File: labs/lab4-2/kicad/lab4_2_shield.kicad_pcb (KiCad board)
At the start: 2 copper layers, 68.6 x 53.3 mm, 35 parts, among them J1 Digital_0-7, J2 Digital_8-13, J3 Power, J4 Analog_In, Q1 2N3904, Q2 2N3904, SW1 SW_Push, SW2 SW_Push, SW3 SW_Push, SW4 SW_Push

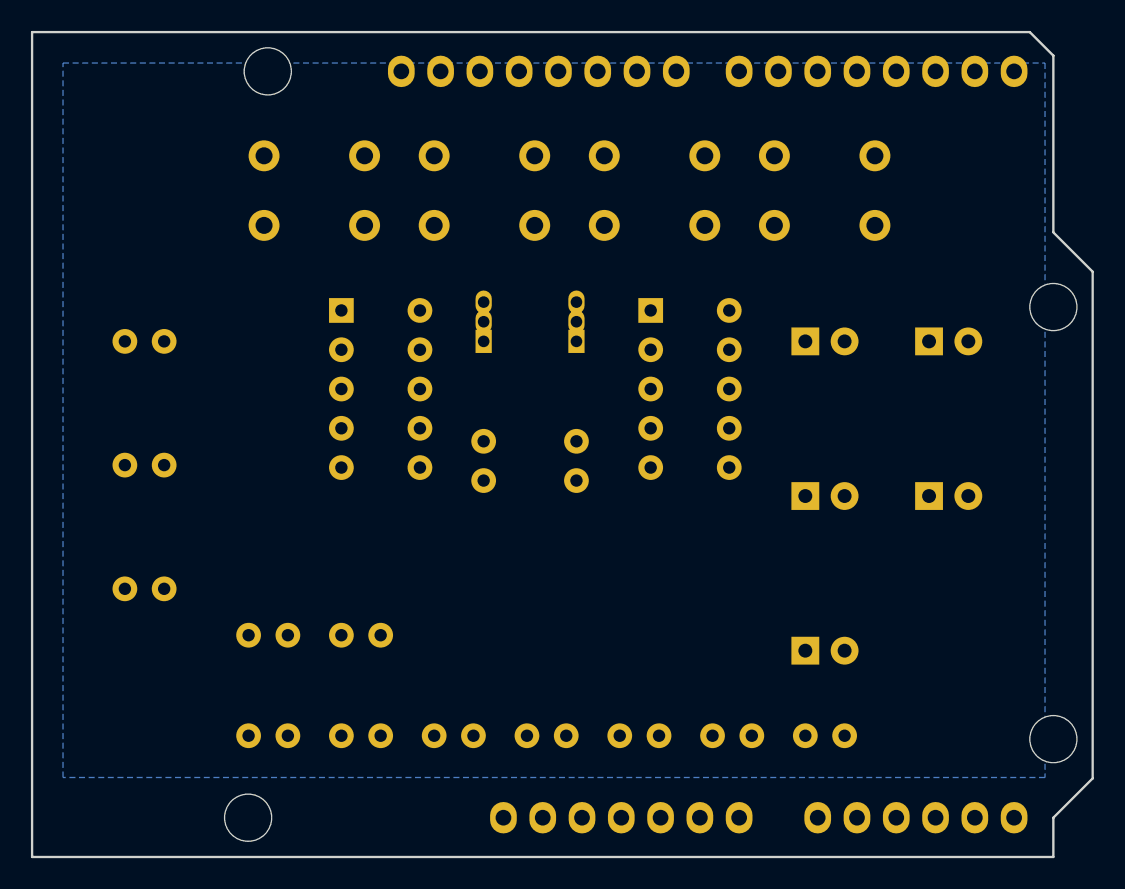
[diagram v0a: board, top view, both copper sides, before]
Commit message: feat: add LTS-6980HR 7-segment display and update KiCad project configurations
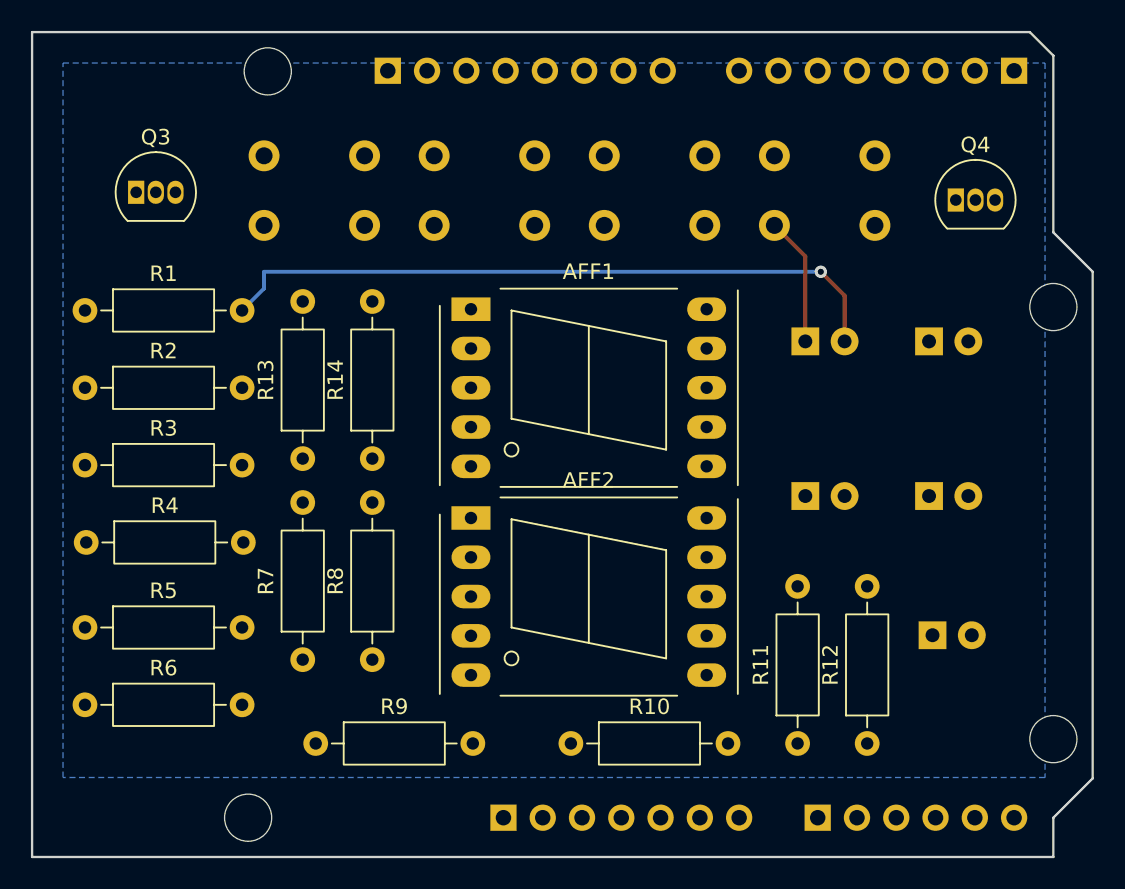
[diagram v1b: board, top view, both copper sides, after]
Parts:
- removed DS1, DS2: 7SEG_CC_GENERIC_VERIFY_PINOUT, lab4_2_shield:DISPLAY_7SEG_CC_GENERIC
- removed Q1, Q2: 2N3904, Package_TO_SOT_THT:TO-92_Inline
- added AFF1: LTS-6980HR, Display_7Segment:7SegmentLED_LTS6760_LTS6780, F.Cu at (128.4, 97.9)
- added AFF2: LTS-6980HR, Display_7Segment:7SegmentLED_LTS6760_LTS6780, F.Cu at (128.4, 111.4)
- added Q3: 2N3904, Package_TO_SOT_THT:TO-92_Inline, F.Cu at (106.7, 90.4)
- added Q4: 2N3904, Package_TO_SOT_THT:TO-92_Inline, F.Cu at (159.7, 90.9)
- J1, J2: footprint lab4_2_shield:Header_Shield_Female_1x08_P2.54mm -> Connector_PinHeader_2.54mm:PinHeader_1x08_P2.54mm_Vertical; moved to B.Cu
- J3: footprint lab4_2_shield:Header_Shield_Female_1x07_P2.54mm -> Connector_PinHeader_2.54mm:PinHeader_1x07_P2.54mm_Vertical; moved to B.Cu
- J4: footprint lab4_2_shield:Header_Shield_Female_1x06_P2.54mm -> Connector_PinHeader_2.54mm:PinHeader_1x06_P2.54mm_Vertical; moved to B.Cu
- R1, R10, R11, R12, R13, R14, R2, R3, R4, R5, R6, R7, R8, R9: footprint Resistor_THT:R_Axial_DIN0207_L6.3mm_D2.5mm_P2.54mm_Vertical -> Resistor_THT:R_Axial_DIN0207_L6.3mm_D2.5mm_P10.16mm_Horizontal
- moved J1 17.8 mm to (163.5, 82.5), turned to 90 degrees
- moved R5 16.6 mm to (103.4, 118.5)
- moved R9 13.7 mm to (118.3, 126.0)
- moved R14 13.3 mm to (122.0, 107.6)
- moved R4 12.1 mm to (103.5, 113.0)
- moved R13 11.8 mm to (117.5, 107.6)
- moved R6 10.8 mm to (103.4, 123.5)
- moved R3 8.41 mm to (103.4, 108.0)
- moved LED5 8.29 mm to (158.2, 119.0)
- moved R8 6.34 mm to (122.0, 120.6), turned to 90 degrees
- moved R2 5.63 mm to (103.4, 103.0)
- moved R11 5.52 mm to (149.5, 126.0), turned to 90 degrees
- moved R7 5.52 mm to (117.5, 120.6), turned to 90 degrees
- moved R12 4.03 mm to (154.0, 126.0), turned to 90 degrees
- moved R1 3.26 mm to (103.4, 98.0)
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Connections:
- net A0_R6 renamed /A0
- net A1_R7 renamed /A1
- net A2_R8 renamed /A2
- net A3_R9 renamed /A3
- net A4_R10 renamed /A4
- net A5_R11 renamed /A5
- net D10 renamed /D10
- net D11 renamed /D11
- net D12_R13 renamed /D12
- net D13_R14 renamed /D13
- net D2_R12 renamed /D2
- net D3_R1 renamed /D3
- net D4_R2 renamed /D4
- net D5_R3 renamed /D5
- net D6_R4 renamed /D6
- net D7_R5 renamed /D7
- net D8 renamed /D8
- net D9 renamed /D9
- net LED1_A renamed Net-(LED1-A)
- net LED2_A renamed Net-(LED2-A)
- net LED3_A renamed Net-(LED3-A)
- net LED4_A renamed Net-(LED4-A)
- net LED5_A renamed Net-(LED5-A)
- J1 pad 7: (no net) -> unconnected-(J1-Pin_7-Pad7)
- J1 pad 8: (no net) -> unconnected-(J1-Pin_8-Pad8)
- J2 pad 1: (no net) -> unconnected-(J2-Pin_1-Pad1)
- J3 pad 1: (no net) -> unconnected-(J3-Pin_1-Pad1)
- J3 pad 2: (no net) -> unconnected-(J3-Pin_2-Pad2)
- J3 pad 3: (no net) -> unconnected-(J3-Pin_3-Pad3)
- J3 pad 4: (no net) -> unconnected-(J3-Pin_4-Pad4)
- J3 pad 5: (no net) -> unconnected-(J3-Pin_5-Pad5)
- J3 pad 6: (no net) -> unconnected-(J3-Pin_6-Pad6)
- J3 pad 7: (no net) -> unconnected-(J3-Pin_7-Pad7)
- R10 pad 1: SEGBUS_E -> Net-(AFF1-e)
- R11 pad 1: SEGBUS_F -> Net-(AFF1-f)
- R12 pad 1: SEGBUS_G -> Net-(AFF1-g)
- R13 pad 2: Q1_BASE -> Net-(Q3-B)
- R14 pad 2: Q2_BASE -> Net-(Q4-B)
- R6 pad 1: SEGBUS_A -> Net-(AFF1-a)
- R7 pad 1: SEGBUS_B -> Net-(AFF1-b)
- R8 pad 1: SEGBUS_C -> Net-(AFF1-c)
- R9 pad 1: SEGBUS_D -> Net-(AFF1-d)
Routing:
- net Net-(LED1-A): track 0.00 -> 44.2 mm, vias 0 -> 1
- net GND: track 0.00 -> 8.33 mm

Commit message: feat: initialize KiCad project files and PCB layout for lab 4.2 shield
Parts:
- renumbered J2 to J1, J1 to J2, Q3 to Q1, Q4 to Q2, R8 to R10, R7 to R11, R13 to R12, R6 to R13, R12 to R6, R11 to R7, R10 to R8
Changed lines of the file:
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@@
 			(layers "*.Cu" "*.Mask")
 			(remove_unused_layers no)
-			(net "Net-(Q4-B)")
+			(net "Net-(Q2-B)")
 			(pintype "passive")
 		)
@@
 			(layers "*.Cu" "*.Mask")
 			(remove_unused_layers no)
-			(net "Net-(Q4-C)")
+			(net "Net-(Q2-C)")
 			(pinfunction "C.K._3")
 			(pintype "passive")
@@
 			(layers "*.Cu" "*.Mask")
 			(remove_unused_layers no)
-			(net "Net-(Q4-C)")
+			(net "Net-(Q2-C)")
 			(pinfunction "C.K._8")
 			(pintype "passive")
@@
 		(descr "Resistor, Axial_DIN0207 series, Axial, Horizontal, pin pitch=10.16mm, 0.25W = 1/4W, length*diameter=6.3*2.5mm^2, http://cdn-reichelt.de/documents/datenblatt/B400/1_4W%23YAG.pdf")
 		(tags "Resistor Axial_DIN0207 series Axial Horizontal pin pitch 10.16mm 0.25W = 1/4W length 6.3mm diameter 2.5mm")
-		(property "Reference" "R7"
+		(property "Reference" "R11"
 			(at 5.08 -2.37 90)
 			(layer "F.SilkS")
@@
 		(descr "Resistor, Axial_DIN0207 series, Axial, Horizontal, pin pitch=10.16mm, 0.25W = 1/4W, length*diameter=6.3*2.5mm^2, http://cdn-reichelt.de/documents/datenblatt/B400/1_4W%23YAG.pdf")
 		(tags "Resistor Axial_DIN0207 series Axial Horizontal pin pitch 10.16mm 0.25W = 1/4W length 6.3mm diameter 2.5mm")
-		(property "Reference" "R11"
+		(property "Reference" "R7"
 			(at 5.08 -2.37 90)
 			(layer "F.SilkS")
@@
 		(descr "Resistor, Axial_DIN0207 series, Axial, Horizontal, pin pitch=10.16mm, 0.25W = 1/4W, length*diameter=6.3*2.5mm^2, http://cdn-reichelt.de/documents/datenblatt/B400/1_4W%23YAG.pdf")
 		(tags "Resistor Axial_DIN0207 series Axial Horizontal pin pitch 10.16mm 0.25W = 1/4W length 6.3mm diameter 2.5mm")
-		(property "Reference" "R12"
+		(property "Reference" "R6"
 			(at 5.08 -2.37 90)
 			(layer "F.SilkS")
@@
 			(layers "*.Cu" "*.Mask")
 			(remove_unused_layers no)
-			(net "Net-(Q3-C)")
+			(net "Net-(Q1-C)")
 			(pinfunction "C.K._3")
 			(pintype "passive")
@@
 			(layers "*.Cu" "*.Mask")
 			(remove_unused_layers no)
-			(net "Net-(Q3-C)")
+			(net "Net-(Q1-C)")
 			(pinfunction "C.K._8")
 			(pintype "passive")
@@
 		(descr "TO-92 leads in-line, narrow, oval pads, drill 0.75mm (see NXP sot054_po.pdf)")
 		(tags "to-92 sc-43 sc-43a sot54 PA33 transistor")
-		(property "Reference" "Q4"
+		(property "Reference" "Q2"
 			(at 1.27 -3.56 0)
 			(layer "F.SilkS")
@@
 			(layers "*.Cu" "*.Mask")
 			(remove_unused_layers no)
-			(net "Net-(Q4-B)")
+			(net "Net-(Q2-B)")
 			(pinfunction "B_2")
 			(pintype "input")
@@
 			(layers "*.Cu" "*.Mask")
 			(remove_unused_layers no)
-			(net "Net-(Q4-C)")
+			(net "Net-(Q2-C)")
 			(pinfunction "C_3")
 			(pintype "passive")
@@
 		(descr "TO-92 leads in-line, narrow, oval pads, drill 0.75mm (see NXP sot054_po.pdf)")
 		(tags "to-92 sc-43 sc-43a sot54 PA33 transistor")
-		(property "Reference" "Q3"
+		(property "Reference" "Q1"
 			(at 1.27 -3.56 0)
 			(layer "F.SilkS")
@@
 			(layers "*.Cu" "*.Mask")
 			(remove_unused_layers no)
-			(net "Net-(Q3-B)")
+			(net "Net-(Q1-B)")
 			(pinfunction "B_2")
 			(pintype "input")
@@
 			(layers "*.Cu" "*.Mask")
 			(remove_unused_layers no)
-			(net "Net-(Q3-C)")
+			(net "Net-(Q1-C)")
 			(pinfunction "C_3")
 			(pintype "passive")
@@
 		(descr "Resistor, Axial_DIN0207 series, Axial, Horizontal, pin pitch=10.16mm, 0.25W = 1/4W, length*diameter=6.3*2.5mm^2, http://cdn-reichelt.de/documents/datenblatt/B400/1_4W%23YAG.pdf")
 		(tags "Resistor Axial_DIN0207 series Axial Horizontal pin pitch 10.16mm 0.25W = 1/4W length 6.3mm diameter 2.5mm")
-		(property "Reference" "R8"
+		(property "Reference" "R10"
 			(at 5.08 -2.37 90)
 			(layer "F.SilkS")
@@
 		(descr "Resistor, Axial_DIN0207 series, Axial, Horizontal, pin pitch=10.16mm, 0.25W = 1/4W, length*diameter=6.3*2.5mm^2, http://cdn-reichelt.de/documents/datenblatt/B400/1_4W%23YAG.pdf")
 		(tags "Resistor Axial_DIN0207 series Axial Horizontal pin pitch 10.16mm 0.25W = 1/4W length 6.3mm diameter 2.5mm")
-		(property "Reference" "R6"
+		(property "Reference" "R13"
 			(at 5.08 -2.37 0)
 			(layer "F.SilkS")
@@
 		(descr "Resistor, Axial_DIN0207 series, Axial, Horizontal, pin pitch=10.16mm, 0.25W = 1/4W, length*diameter=6.3*2.5mm^2, http://cdn-reichelt.de/documents/datenblatt/B400/1_4W%23YAG.pdf")
 		(tags "Resistor Axial_DIN0207 series Axial Horizontal pin pitch 10.16mm 0.25W = 1/4W length 6.3mm diameter 2.5mm")
-		(property "Reference" "R13"
+		(property "Reference" "R12"
 			(at 5.08 -2.37 90)
 			(layer "F.SilkS")
@@
 			(layers "*.Cu" "*.Mask")
 			(remove_unused_layers no)
-			(net "Net-(Q3-B)")
+			(net "Net-(Q1-B)")
 			(pintype "passive")
 		)
@@
 		(descr "Resistor, Axial_DIN0207 series, Axial, Horizontal, pin pitch=10.16mm, 0.25W = 1/4W, length*diameter=6.3*2.5mm^2, http://cdn-reichelt.de/documents/datenblatt/B400/1_4W%23YAG.pdf")
 		(tags "Resistor Axial_DIN0207 series Axial Horizontal pin pitch 10.16mm 0.25W = 1/4W length 6.3mm diameter 2.5mm")
-		(property "Reference" "R10"
+		(property "Reference" "R8"
 			(at 5.08 -2.37 0)
 			(layer "F.SilkS")
@@
 		(descr "Through hole straight pin header, 1x08, 2.54mm pitch, single row")
 		(tags "Through hole pin header THT 1x08 2.54mm single row")
-		(property "Reference" "J1"
+		(property "Reference" "J2"
 			(at 0 2.38 270)
 			(layer "B.SilkS")
@@
 			(layers "*.Cu" "*.Mask")
 			(remove_unused_layers no)
-			(net "unconnected-(J1-Pin_7-Pad7)")
+			(net "unconnected-(J2-Pin_7-Pad7)")
 			(pinfunction "Pin_7_7")
 			(pintype "passive+no_connect")
@@
 			(layers "*.Cu" "*.Mask")
 			(remove_unused_layers no)
-			(net "unconnected-(J1-Pin_8-Pad8)")
+			(net "unconnected-(J2-Pin_8-Pad8)")
 			(pinfunction "Pin_8_8")
 			(pintype "passive+no_connect")
@@
 		(descr "Through hole straight pin header, 1x08, 2.54mm pitch, single row")
 		(tags "Through hole pin header THT 1x08 2.54mm single row")
-		(property "Reference" "J2"
+		(property "Reference" "J1"
 			(at 0 2.38 90)
 			(layer "B.SilkS")
@@
 			(layers "*.Cu" "*.Mask")
 			(remove_unused_layers no)
-			(net "unconnected-(J2-Pin_1-Pad1)")
+			(net "unconnected-(J1-Pin_1-Pad1)")
 			(pinfunction "Pin_1_1")
 			(pintype "passive+no_connect")

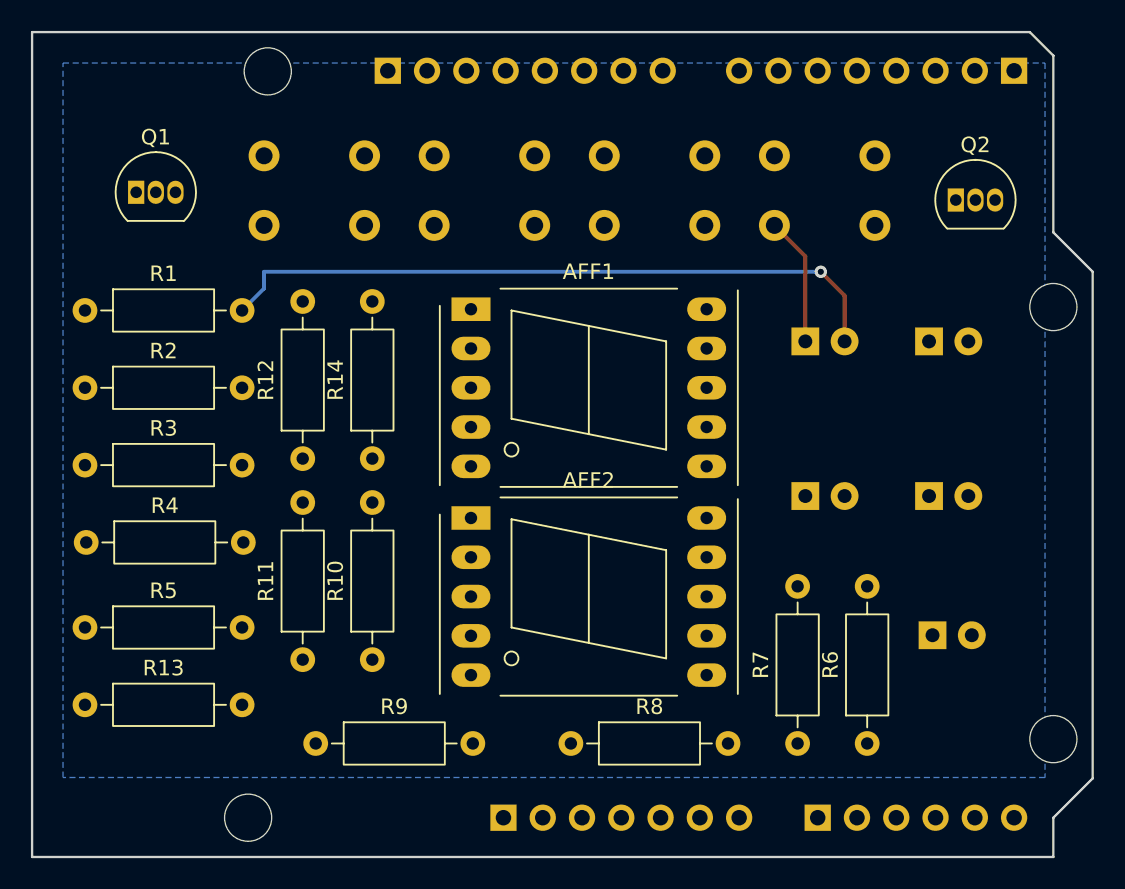
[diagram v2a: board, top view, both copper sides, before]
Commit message: refactor: update text label coordinates and component placements in KiCad project files
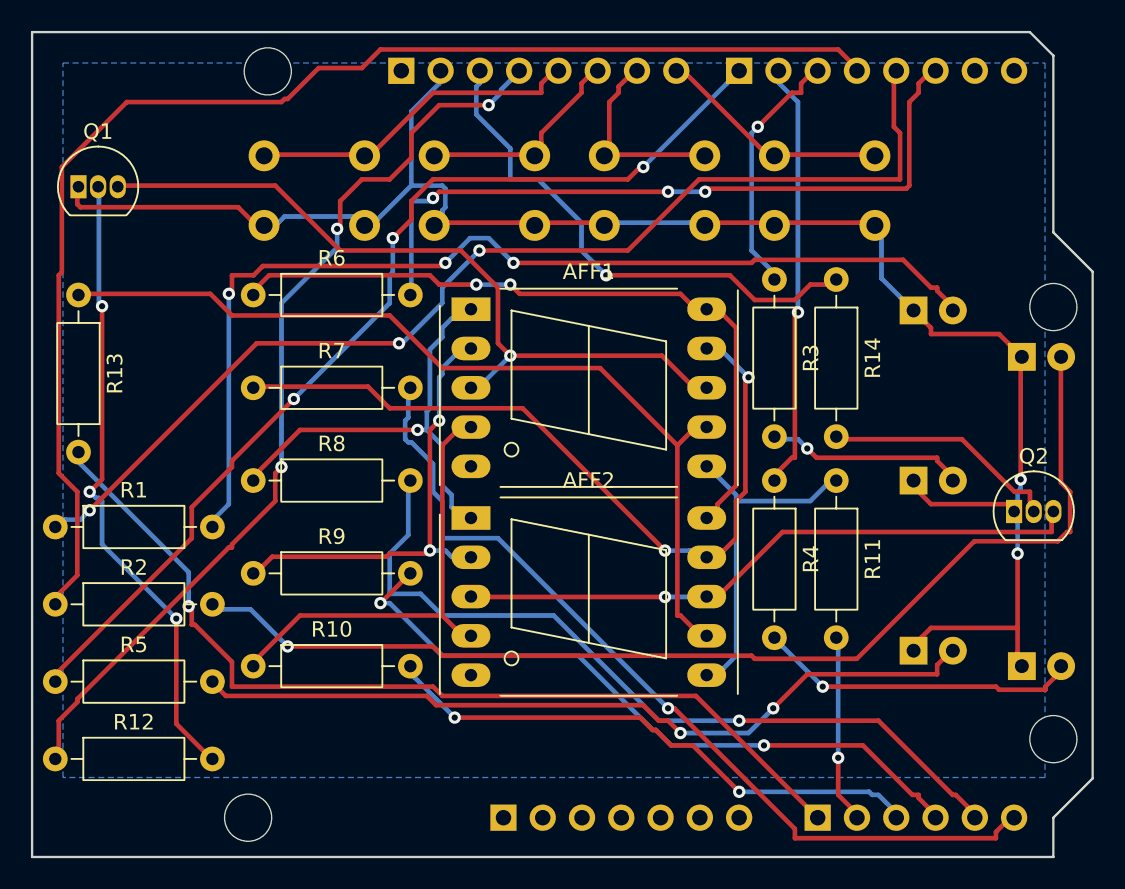
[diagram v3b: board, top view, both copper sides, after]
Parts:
- moved R6 49.2 mm to (114.3, 97.0), turned to 0 degrees
- moved R3 46.2 mm to (148.0, 96.0), turned to -90 degrees
- moved R4 44.7 mm to (148.0, 109.0), turned to -90 degrees
- moved R7 42.0 mm to (114.3, 103.0), turned to 0 degrees
- moved R11 36.4 mm to (152.0, 109.0), turned to -90 degrees
- moved R14 32.2 mm to (152.0, 96.0), turned to -90 degrees
- moved R8 26.7 mm to (114.3, 109.0)
- moved R13 26.5 mm to (103.0, 97.0), turned to -90 degrees
- moved R12 25.2 mm to (101.5, 127.0), turned to 0 degrees
- moved Q2 20.5 mm to (163.5, 111.0)
- moved J2 17.8 mm to (145.7, 82.5), turned to -90 degrees
- moved R1 14.1 mm to (101.5, 112.0)
- moved R2 14.1 mm to (101.5, 117.0)
- moved LED4 12.5 mm to (164.0, 121.0)
- moved R9 11.7 mm to (114.3, 115.0)
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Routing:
- net GND: track 8.33 -> 116.5 mm, vias 0 -> 2
- net /D4: track 0.00 -> 84.6 mm
- net Net-(LED2-A): track 0.00 -> 71.8 mm, vias 0 -> 1
- net /D3: track 0.00 -> 71.7 mm, vias 0 -> 3
- net /D7: track 0.00 -> 65.2 mm, vias 0 -> 3
- net /A0: track 0.00 -> 60.7 mm, vias 0 -> 1
- net /D12: track 0.00 -> 59.9 mm, vias 0 -> 3
- net Net-(AFF1-a): track 0.00 -> 58.4 mm
- net /A5: track 0.00 -> 57.0 mm, vias 0 -> 1
- net Net-(LED5-A): track 0.00 -> 51.8 mm, vias 0 -> 2
- net /A4: track 0.00 -> 51.8 mm, vias 0 -> 1
- net Net-(AFF1-f): track 0.00 -> 50.2 mm, vias 0 -> 2
- net Net-(Q1-C): track 0.00 -> 48.9 mm, vias 0 -> 1
- net /D2: track 0.00 -> 46.9 mm, vias 0 -> 3
- net Net-(AFF1-g): track 0.00 -> 46.2 mm, vias 0 -> 2
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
